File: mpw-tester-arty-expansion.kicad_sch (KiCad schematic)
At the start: 112 parts, among them J1 USB4105-GF-A, J10 61300211121, J11 61300211121, J12 61300211121, J14 61300311121, J15 61300311121, J18 61300411121, J19 61300711121, J20 61300411121, J3 Arty_A7_SPI, J4 61300211121, J5 61300311121, J6 61300211121, J7 61300211121, J8 61300211121, J9 61300211121, Q1 DTC014TEBTL, SW1 JS202011JCQN, U1 SN74LVC1G125DCKR, U2 FT232HQ, U3 SN74LVC1G125DCKR, U4 MAX811REUS+T, U5 NTS0102DP, U6 MCP4661-103E/ML, U7 Caravel_breakout_PCB, U8 W25Q32FVSS, U9 MIC2211-AAYML-TR, Y1 ABM8G-12.000MHZ-18-D2Y-T, Y2 ECS-2520MVLC-100-BN-TR

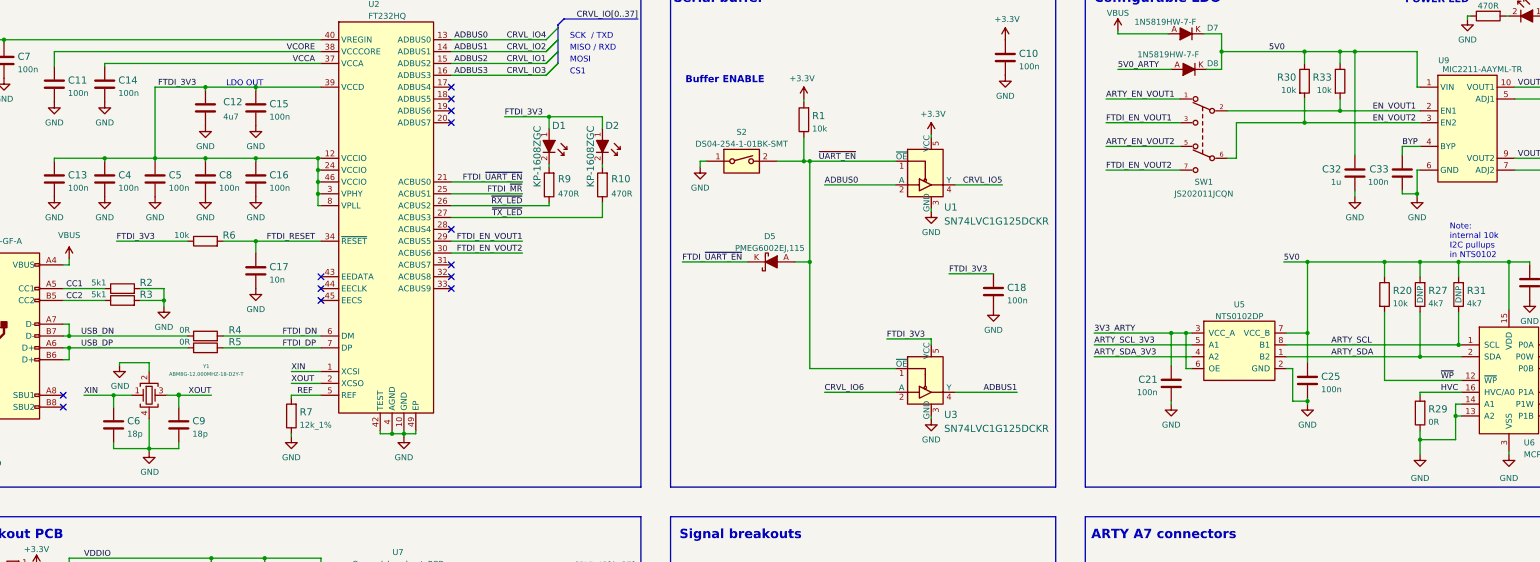
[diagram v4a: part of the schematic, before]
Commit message: Add slide switches for Arty powered from USB and UART buffer ctrl
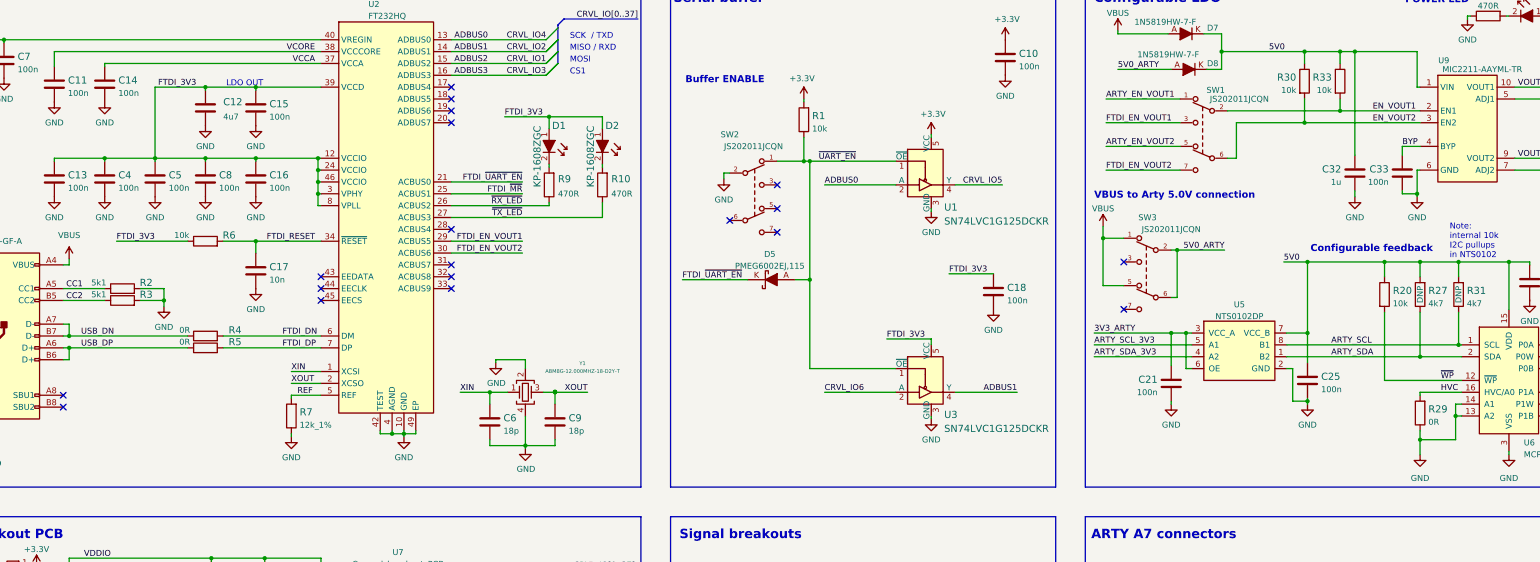
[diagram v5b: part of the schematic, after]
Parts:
- removed S2: DS04-254-1-01BK-SMT, antmicro-footprints:SW_DS04-254-1-01BK-SMT, symbol antmicroSlideSwitches:DS04-254-1-01BK-SMT
- added SW2, SW3: JS202011JCQN, antmicro-footprints:JS202011JCQN, symbol antmicroSlideSwitches:JS202011JCQN
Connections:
- net 5V0_ARTY: now also SW3.2 (1_C), SW3.6 (2_C)
- net AGND: now also SW2.2 (1_C)
- net VBUS: now also SW3.1, SW3.5
- net ~{UART_EN}: now also SW2.1
- no-connect marks 21 -> 27
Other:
- note added: "Configurable feedback"
- note added: "VBUS to Arty 5.0V connection"
- moved on the sheet: C6, C9, D5, Y1

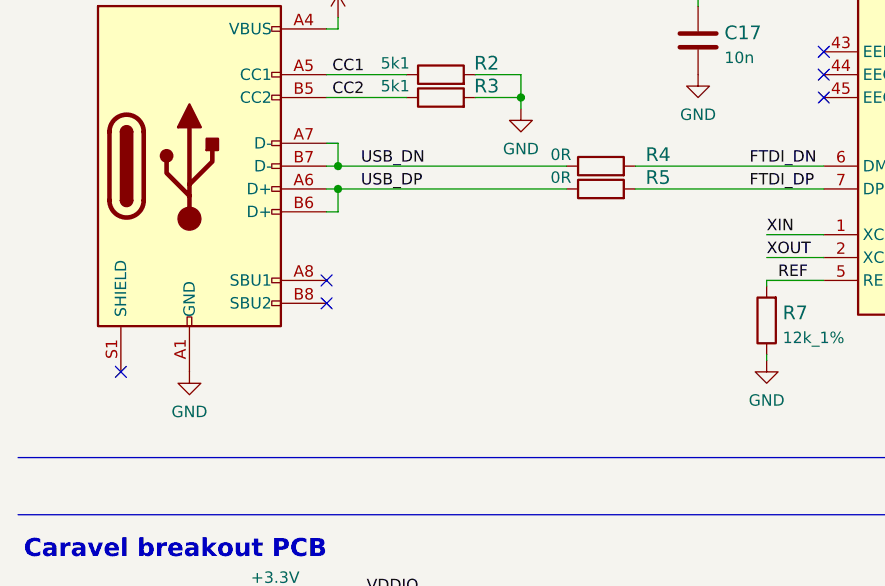
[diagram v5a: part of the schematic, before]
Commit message: Add USB TVS, finish layout, resolve DRC
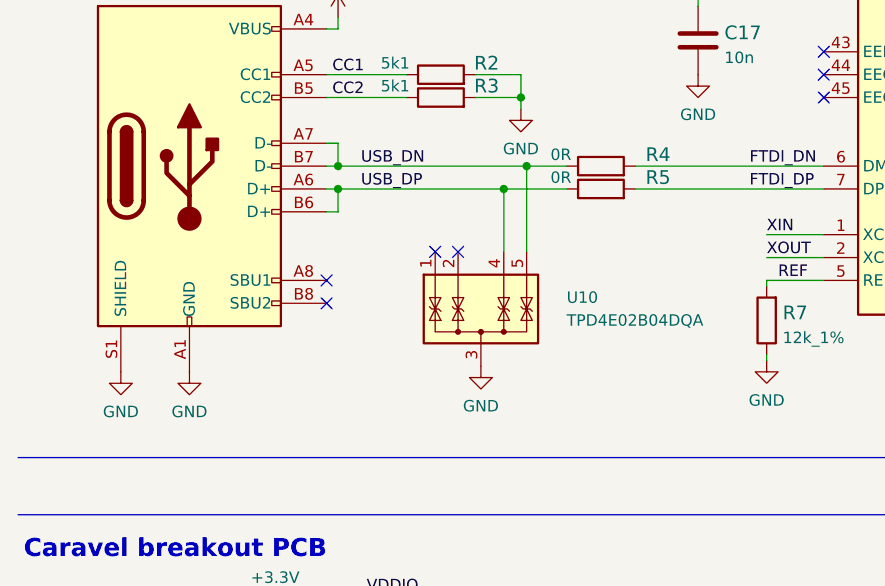
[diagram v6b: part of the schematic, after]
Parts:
- added U10: TPD4E02B04DQA, antmicro-footprints:USON-10_2.5x1.0mm_P0.5mm, symbol antmicroTVSDiodes:TPD4E02B04DQA
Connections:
- net AGND: now also J1.S1 (SHIELD), U10.3 (G), U10.8 (G)
- net USB_DN: now also U10.5 (IO4), U10.6 (NC)
- net USB_DP: now also U10.4 (IO3), U10.7 (NC)
- new net: U10.1 (IO1), U10.10 (NC)
- new net: U10.2 (IO2), U10.9 (NC)
- no-connect marks 27 -> 28
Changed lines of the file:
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@@
   (junction (at 79.375 173.355) (diameter 0) (color 0 0 0 0)
   )
+  (junction (at 69.85 88.265) (diameter 0) (color 0 0 0 0)
+  )
   (junction (at 79.375 262.255) (diameter 0) (color 0 0 0 0)
   )
@@
   (junction (at 67.945 155.575) (diameter 0) (color 0 0 0 0)
   )
+  (junction (at 67.31 90.805) (diameter 0) (color 0 0 0 0)
+  )
   (junction (at 151.765 41.275) (diameter 0) (color 0 0 0 0)
   )
@@
   (junction (at 313.69 27.305) (diameter 0) (color 0 0 0 0)
   )
-  (no_connect (at 24.765 111.125))
+  (no_connect (at 59.69 97.79))
   (no_connect (at 291.465 163.195))
   (no_connect (at 386.08 90.17))
@@
   (no_connect (at 130.81 75.565))
   (no_connect (at 130.81 34.925))
+  (no_connect (at 62.23 97.79))
   (no_connect (at 200.66 55.88))
   (no_connect (at 190.5 63.5))
@@
     (stroke (width 0) (type default) (color 0 0 0 0))
   )
+  (wire (pts (xy 67.31 90.805) (xy 74.295 90.805))
+    (stroke (width 0) (type default) (color 0 0 0 0))
+  )
   (bus (pts (xy 224.155 177.8) (xy 224.155 180.34))
     (stroke (width 0) (type default) (color 0 0 0 0))
@@
     (stroke (width 0) (type default) (color 0 0 0 0))
   )
-  (wire (pts (xy 48.895 88.265) (xy 74.295 88.265))
+  (wire (pts (xy 48.895 88.265) (xy 69.85 88.265))
     (stroke (width 0) (type default) (color 0 0 0 0))
   )
@@
     (stroke (width 0) (type default) (color 0 0 0 0))
   )
+  (wire (pts (xy 67.31 90.805) (xy 67.31 97.79))
+    (stroke (width 0) (type default) (color 0 0 0 0))
+  )
   (wire (pts (xy 59.055 259.715) (xy 60.325 259.715))
     (stroke (width 0) (type default) (color 0 0 0 0))
@@
     (stroke (width 0) (type default) (color 0 0 0 0))
   )
+  (wire (pts (xy 69.85 88.265) (xy 74.295 88.265))
+    (stroke (width 0) (type default) (color 0 0 0 0))
+  )
   (wire (pts (xy 48.895 90.805) (xy 47.625 90.805))
     (stroke (width 0) (type default) (color 0 0 0 0))
@@
     (stroke (width 0) (type default) (color 0 0 0 0))
   )
+  (wire (pts (xy 69.85 88.265) (xy 69.85 97.79))
+    (stroke (width 0) (type default) (color 0 0 0 0))
+  )
   (wire (pts (xy 227.33 147.32) (xy 245.11 147.32))
     (stroke (width 0) (type default) (color 0 0 0 0))
@@
     (stroke (width 0) (type default) (color 0 0 0 0))
   )
-  (wire (pts (xy 48.895 90.805) (xy 74.295 90.805))
+  (wire (pts (xy 48.895 90.805) (xy 67.31 90.805))
     (stroke (width 0) (type default) (color 0 0 0 0))
   )
@@
     (pin "1")
   )
+  (symbol (lib_id "power:GND") (at 24.765 111.125 0) (unit 1)
+    (in_bom yes) (on_board yes) (fields_autoplaced)
+    (property "Reference" "#PWR?" (id 0) (at 24.765 117.475 0)
+      (effects (font (size 1.27 1.27)) hide)
+    )
+    (property "Value" "GND" (id 1) (at 24.765 115.57 0))
+    (property "Footprint" "" (id 2) (at 24.765 111.125 0)
+      (effects (font (size 1.27 1.27)) hide)
+    )
+    (property "Datasheet" "" (id 3) (at 24.765 111.125 0)
+      (effects (font (size 1.27 1.27)) hide)
+    )
+    (pin "1")
+  )
   (symbol (lib_id "power:GND") (at 97.155 271.145 0) (unit 1)
     (in_bom yes) (on_board yes) (fields_autoplaced)
@@
     (pin "2")
   )
+  (symbol (lib_id "power:GND") (at 64.77 110.49 0) (unit 1)
+    (in_bom yes) (on_board yes) (fields_autoplaced)
+    (property "Reference" "#PWR0151" (id 0) (at 64.77 116.84 0)
+      (effects (font (size 1.27 1.27)) hide)
+    )
+    (property "Value" "GND" (id 1) (at 64.77 114.935 0))
+    (property "Footprint" "" (id 2) (at 64.77 110.49 0)
+      (effects (font (size 1.27 1.27)) hide)
+    )
+    (property "Datasheet" "" (id 3) (at 64.77 110.49 0)
+      (effects (font (size 1.27 1.27)) hide)
+    )
+    (pin "1")
+  )
   (symbol (lib_id "power:GND") (at 243.84 156.21 0) (mirror y) (unit 1)
     (in_bom yes) (on_board yes)
@@
     (pin "2")
   )
+  (symbol (lib_id "antmicroTVSDiodes:TPD4E02B04DQA") (at 64.77 105.41 0) (unit 1)
+    (in_bom yes) (on_board yes) (fields_autoplaced)
+    (property "Reference" "U10" (id 0) (at 74.295 102.8699 0)
+      (effects (font (size 1.27 1.27)) (justify left))
+    )
+    (property "Value" "TPD4E02B04DQA" (id 1) (at 74.295 105.4099 0)
+      (effects (font (size 1.27 1.27)) (justify left))
+    )
+    (property "Footprint" "antmicro-footprints:USON-10_2.5x1.0mm_P0.5mm" (id 2) (at 52.07 128.27 0)
+      (effects (font (size 1.27 1.27)) (justify left) hide)
+    )
+    (property "Datasheet" "http://www.ti.com/lit/ds/symlink/tpd4e02b04.pdf" (id 3) (at 64.77 125.73 0)
+      (effects (font (size 1.27 1.27)) hide)
+    )
+    (property "MPN" "TPD4E02B04DQAR" (id 4) (at 64.77 120.65 0)
+      (effects (font (size 1.27 1.27)) hide)
+    )
+    (property "Manufacturer" "Texas Instruments" (id 5) (at 64.77 123.19 0)
+      (effects (font (size 1.27 1.27)) hide)
+    )
+    (pin "3")
+    (pin "1")
+    (pin "10")
+    (pin "2")
+    (pin "4")
+    (pin "5")
+    (pin "6")
+    (pin "7")
+    (pin "8")
+    (pin "9")
+  )
   (symbol (lib_id "antmicroCapacitors0603:C_1u_0603") (at 90.805 182.88 0) (unit 1)
     (in_bom yes) (on_board yes) (fields_autoplaced)
@@
       (reference "#PWR0150") (unit 1) (value "GND") (footprint "")
     )
+    (path "/7c3d5220-0c26-4068-8fa2-00d0fffbad0b"
+      (reference "#PWR0151") (unit 1) (value "GND") (footprint "")
+    )
     (path "/3349caa0-d316-426d-823b-0e2b9b5356e8"
       (reference "#PWR0152") (unit 1) (value "GND") (footprint "")
@@
       (reference "#PWR0180") (unit 1) (value "GND") (footprint "")
     )
+    (path "/07aae223-3c13-41d7-a3d8-dbdee37fc036"
+      (reference "#PWR?") (unit 1) (value "GND") (footprint "")
+    )
     (path "/c364c452-410a-49be-b768-048ab800dd72"
       (reference "C1") (unit 1) (value "C_1u_0603") (footprint "antmicro-footprints:0603-cap")
@@
       (reference "U9") (unit 1) (value "MIC2211-AAYML-TR") (footprint "antmicro-footprints:DFN-10-1EP_3x3mm")
     )
+    (path "/df40db42-563e-400d-856d-2e4e6bd95abf"
+      (reference "U10") (unit 1) (value "TPD4E02B04DQA") (footprint "antmicro-footprints:USON-10_2.5x1.0mm_P0.5mm")
+    )
     (path "/90785e37-9e70-447f-a70d-a3ed142c95ed"

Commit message: Loclib
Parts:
- C1, C22, C23, C24, C26, C27, C28, C29, C3, C30, C31, C32, C35, C36: footprint antmicro-footprints:0603-cap -> mpw-tester-arty-expansion-footprints:0603-cap; symbol antmicroCapacitors0603:C_1u_0603 -> mpw-tester-arty-expansion:C_1u_0603
- C10, C11, C13, C14, C15, C16, C18, C19, C20, C21, C25, C33, C34, C37, C4, C5, C7, C8: footprint antmicro-footprints:0603-cap -> mpw-tester-arty-expansion-footprints:0603-cap; symbol antmicroCapacitors0603:C_100n_0603 -> mpw-tester-arty-expansion:C_100n_0603
- C12, C2: footprint antmicro-footprints:0603-cap -> mpw-tester-arty-expansion-footprints:0603-cap; symbol antmicroCapacitors0603:C_4u7_0603 -> mpw-tester-arty-expansion:C_4u7_0603
- C17: footprint antmicro-footprints:0603-cap -> mpw-tester-arty-expansion-footprints:0603-cap; symbol antmicroCapacitors0603:C_10n_0603 -> mpw-tester-arty-expansion:C_10n_0603
- C6, C9: footprint antmicro-footprints:0603-cap -> mpw-tester-arty-expansion-footprints:0603-cap; symbol antmicroCapacitors0603:C_18p_0603 -> mpw-tester-arty-expansion:C_18p_0603
- D1, D2, D3, D4: footprint antmicro-footprints:LED_0603 -> mpw-tester-arty-expansion-footprints:LED_0603; symbol antmicroLEDIndicationDiscrete:KP-1608ZGC -> mpw-tester-arty-expansion:KP-1608ZGC
- D5, D6, D9: footprint antmicro-footprints:SOD-323F -> mpw-tester-arty-expansion-footprints:SOD-323F; symbol antmicroDiodesRectifiersSingle:PMEG6002EJ,115 -> mpw-tester-arty-expansion:PMEG6002EJ,115
- D7, D8: footprint antmicro-footprints:SOD-123 -> mpw-tester-arty-expansion-footprints:SOD-123; symbol antmicroDiodesRectifiersSingle:1N5819HW-7-F -> mpw-tester-arty-expansion:1N5819HW-7-F
- J1: footprint antmicro-footprints:GCT_USB4105-GF-A -> mpw-tester-arty-expansion-footprints:GCT_USB4105-GF-A; symbol antmicroUSBDVIHDMIConnectors:USB4105-GF-A -> mpw-tester-arty-expansion:USB4105-GF-A
- J10, J11, J12, J4, J6, J7, J8, J9: footprint antmicro-footprints:PinHeader_1x2_P2.54_Drill0.9mm -> mpw-tester-arty-expansion-footprints:PinHeader_1x2_P2.54_Drill0.9mm; symbol antmicroRectangularConnectorsHeadersMalePins:61300211121 -> mpw-tester-arty-expansion:61300211121
- J14, J15, J5: footprint antmicro-footprints:PinHeader_1x3_P2.54_Drill1.1mm -> mpw-tester-arty-expansion-footprints:PinHeader_1x3_P2.54_Drill1.1mm; symbol antmicroRectangularConnectorsHeadersMalePins:61300311121 -> mpw-tester-arty-expansion:61300311121
- J18, J20: footprint antmicro-footprints:PinHeader_1x4_P2.54mm_Drill1.02mm -> mpw-tester-arty-expansion-footprints:PinHeader_1x4_P2.54mm_Drill1.02mm; symbol antmicroRectangularConnectorsHeadersMalePins:61300411121 -> mpw-tester-arty-expansion:61300411121
- J19: footprint antmicro-footprints:61300711121 -> mpw-tester-arty-expansion-footprints:61300711121; symbol antmicroRectangularConnectorsHeadersMalePins:61300711121 -> mpw-tester-arty-expansion:61300711121
- J3: footprint antmicro-footprints:ARTY_A7_SHIELD -> mpw-tester-arty-expansion-footprints:ARTY_A7_SHIELD; symbol antmicroRectangularConnectorsHeadersMalePins:Arty_A7_SPI -> mpw-tester-arty-expansion:Arty_A7_SPI
- Q1: footprint antmicro-footprints:SOT-416 -> mpw-tester-arty-expansion-footprints:SOT-416; symbol antmicroTransistorsBipolarSingle:DTC014TEBTL -> mpw-tester-arty-expansion:DTC014TEBTL
- R1, R16, R17, R18, R19, R20, R21, R26, R28, R30, R32, R33, R34, R6: footprint antmicro-footprints:0603-res -> mpw-tester-arty-expansion-footprints:0603-res; symbol antmicroResistors0603:R_10k_0603 -> mpw-tester-arty-expansion:R_10k_0603
- R10, R12, R13, R9: footprint antmicro-footprints:0603-res -> mpw-tester-arty-expansion-footprints:0603-res; symbol antmicroResistors0603:R_470R_0603 -> mpw-tester-arty-expansion:R_470R_0603
- R11, R14, R15, R29, R8: footprint antmicro-footprints:0603-res -> mpw-tester-arty-expansion-footprints:0603-res; symbol antmicroResistors0603:R_0R_0603 -> mpw-tester-arty-expansion:R_0R_0603
- R2, R3: footprint antmicro-footprints:0603-res -> mpw-tester-arty-expansion-footprints:0603-res; symbol antmicroResistors0603:R_5k1_0603 -> mpw-tester-arty-expansion:R_5k1_0603
- R22: footprint antmicro-footprints:0603-res -> mpw-tester-arty-expansion-footprints:0603-res; symbol antmicroResistors0603:R_68k_0603 -> mpw-tester-arty-expansion:R_68k_0603
- R23: footprint antmicro-footprints:0603-res -> mpw-tester-arty-expansion-footprints:0603-res; symbol antmicroResistors0603:R_41k2_0603 -> mpw-tester-arty-expansion:R_41k2_0603
- R24: footprint antmicro-footprints:0603-res -> mpw-tester-arty-expansion-footprints:0603-res; symbol antmicroResistors0603:R_15k_0603 -> mpw-tester-arty-expansion:R_15k_0603
- R25: footprint antmicro-footprints:0603-res -> mpw-tester-arty-expansion-footprints:0603-res; symbol antmicroResistors0603:R_34k_0603 -> mpw-tester-arty-expansion:R_34k_0603
- R27, R31: footprint antmicro-footprints:0603-res -> mpw-tester-arty-expansion-footprints:0603-res; symbol antmicroResistors0603:R_4k7_0603 -> mpw-tester-arty-expansion:R_4k7_0603
- R4, R5: footprint antmicro-footprints:0402-res -> mpw-tester-arty-expansion-footprints:0402-res; symbol antmicroResistors0402:R_0R_0402 -> mpw-tester-arty-expansion:R_0R_0402
- R7: footprint antmicro-footprints:0603-res -> mpw-tester-arty-expansion-footprints:0603-res; symbol antmicroResistors0603:R_12k_1%_0603 -> mpw-tester-arty-expansion:R_12k_1%_0603
- S1: footprint antmicro-footprints:SW_SPST_4.2x2.8 -> mpw-tester-arty-expansion-footprints:SW_SPST_4.2x2.8; symbol antmicroPushbuttonSwitches:KMR2 -> mpw-tester-arty-expansion:KMR2
- SW1, SW2, SW3: footprint antmicro-footprints:JS202011JCQN -> mpw-tester-arty-expansion-footprints:JS202011JCQN; symbol antmicroSlideSwitches:JS202011JCQN -> mpw-tester-arty-expansion:JS202011JCQN
- TP1: footprint antmicro-footprints:PROBE_PAD_1206 -> mpw-tester-arty-expansion-footprints:PROBE_PAD_1206; symbol antmicroTestPoints:RCW-0C -> mpw-tester-arty-expansion:RCW-0C
- U1, U3: footprint antmicro-footprints:SOT-353 -> mpw-tester-arty-expansion-footprints:SOT-353; symbol antmicroLogicBuffersDriversReceiversTransceivers:SN74LVC1G125DCKR -> mpw-tester-arty-expansion:SN74LVC1G125DCKR
- U10: footprint antmicro-footprints:USON-10_2.5x1.0mm_P0.5mm -> mpw-tester-arty-expansion-footprints:USON-10_2.5x1.0mm_P0.5mm; symbol antmicroTVSDiodes:TPD4E02B04DQA -> mpw-tester-arty-expansion:TPD4E02B04DQA
- U2: footprint antmicro-footprints:QFN-48-1EP_8x8mm_P0.5mm_EP6.2x6.2mm_FT232HQ_marking -> mpw-tester-arty-expansion-footprints:QFN-48-1EP_8x8mm_P0.5mm_EP6.2x6.2mm_FT232HQ_marking; symbol antmicroInterfaceControllers:FT232HQ -> mpw-tester-arty-expansion:FT232HQ
- U4: footprint antmicro-footprints:SOT-143-4 -> mpw-tester-arty-expansion-footprints:SOT-143-4; symbol antmicroPMICPowerSequencers:MAX811REUS+T -> mpw-tester-arty-expansion:MAX811REUS+T
- U5: footprint antmicro-footprints:TSSOP-8_W3mm -> mpw-tester-arty-expansion-footprints:TSSOP-8_W3mm; symbol antmicroLogicTranslatorsLevelShifters:NTS0102DP -> mpw-tester-arty-expansion:NTS0102DP
- U6: footprint antmicro-footprints:QFN-16_EP_4x4_Pitch0.65mm -> mpw-tester-arty-expansion-footprints:QFN-16_EP_4x4_Pitch0.65mm; symbol antmicroInterfaceIOExpanders:MCP4661-103E/ML -> mpw-tester-arty-expansion:MCP4661-103E/ML
- U7: footprint antmicro-footprints:caravel_breakout -> mpw-tester-arty-expansion-footprints:caravel_breakout; symbol antmicroModules:Caravel_breakout_PCB -> mpw-tester-arty-expansion:Caravel_breakout_PCB
- U8: footprint antmicro-footprints:SOIC127P790X216-8N -> mpw-tester-arty-expansion-footprints:SOIC127P790X216-8N; symbol antmicroMemory:W25Q32FVSS -> mpw-tester-arty-expansion:W25Q32FVSS
- U9: footprint antmicro-footprints:DFN-10-1EP_3x3mm -> mpw-tester-arty-expansion-footprints:DFN-10-1EP_3x3mm; symbol antmicroPMICVoltageRegulatorsLinear:MIC2211-AAYML-TR -> mpw-tester-arty-expansion:MIC2211-AAYML-TR
- Y1: footprint antmicro-footprints:KX-7 -> mpw-tester-arty-expansion-footprints:KX-7; symbol antmicroCrystals:ABM8G-12.000MHZ-18-D2Y-T -> mpw-tester-arty-expansion:ABM8G-12.000MHZ-18-D2Y-T
- Y2: footprint antmicro-footprints:Oscillator_SMD_ECS_2520MV-xxx-xx-4Pin_2.5x2.0mm -> mpw-tester-arty-expansion-footprints:Oscillator_SMD_ECS_2520MV-xxx-xx-4Pin_2.5x2.0mm; symbol antmicroCrystals:ECS-2520MVLC-100-BN-TR -> mpw-tester-arty-expansion:ECS-2520MVLC-100-BN-TR
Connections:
- net ADBUS0: no longer J3.35 (IO37)
- net ADBUS1: no longer J3.34 (IO38)
- net ADBUS2: no longer J3.51 (IO13)
- net ADBUS3: no longer J3.52 (IO12)
- net ARTY_SCL_3V3: no longer J3.47 (SCL)
- net ARTY_SDA_3V3: no longer J3.48 (SDA)
- net ARTY_XCLK: no longer J3.32 (IO40)
- net ARTY_~{MR}: no longer J3.31 (IO41)
- net CRVL_IO0: no longer J3.33 (IO39)
- net CRVL_IO10: no longer J3.38 (IO34)
- net CRVL_IO11: no longer J3.56 (IO08)
- net CRVL_IO12: no longer J3.39 (IO33)
- net CRVL_IO13: no longer J3.57 (IO07)
- net CRVL_IO14: no longer J3.40 (IO32)
- net CRVL_IO15: no longer J3.58 (IO06)
- net CRVL_IO16: no longer J3.41 (IO31)
- net CRVL_IO17: no longer J3.59 (IO05)
- net CRVL_IO18: no longer J3.42 (IO30)
- net CRVL_IO19: no longer J3.60 (IO04)
- net CRVL_IO20: no longer J3.43 (IO29)
- net CRVL_IO21: no longer J3.61 (IO03)
- net CRVL_IO22: no longer J3.44 (IO28)
- net CRVL_IO23: no longer J3.62 (IO02)
- net CRVL_IO24: no longer J3.45 (IO27)
- net CRVL_IO25: no longer J3.63 (IO01)
- net CRVL_IO26: no longer J3.46 (IO26)
- net CRVL_IO27: no longer J3.64 (IO00)
- net CRVL_IO5: no longer J3.53 (IO11)
- net CRVL_IO6: no longer J3.36 (IO36)
- net CRVL_IO7: no longer J3.54 (IO10)
- net CRVL_IO8: no longer J3.37 (IO35)
- net CRVL_IO9: no longer J3.55 (IO09)

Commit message: Fix Arty symbol, add EP pin to MIC221 and MCP4661 symbols
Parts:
- removed J3: Arty_A7_SPI, mpw-tester-arty-expansion-footprints:ARTY_A7_SHIELD, symbol mpw-tester-arty-expansion:Arty_A7_SPI
- added J3: arty_chipKIT_connector, mpw-tester-arty-expansion-footprints:ARTY_A7_SHIELD, symbol mpw-tester-arty-expansion:arty_chipKIT_connector
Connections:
- net 3V3_ARTY: now also J3.4 (3V3)
- net 5V0_ARTY: now also J3.5 (5V)
- net ADBUS0: now also J3.35 (IO37)
- net ADBUS1: now also J3.34 (IO38)
- net ADBUS2: now also J3.51 (IO13)
- net ADBUS3: now also J3.52 (IO12)
- net AGND: now also U6.17 (EP), U9.11 (EP), J3.17 (XGND), J3.26 (GND), J3.6 (GND), J3.7 (GND)
- net ARTY_EN_VOUT1: now also J3.9 (A0)
- net ARTY_EN_VOUT2: now also J3.19 (A6)
- net ARTY_MEM_CS: now also J3.25 (SS)
- net ARTY_MEM_MISO: now also R14.1, J3.28 (MISO); no longer R15.1
- net ARTY_MEM_MOSI: now also R15.1, J3.29 (MOSI); no longer R14.1
- net ARTY_MEM_SCK: now also J3.27 (SCK)
- net ARTY_SCL_3V3: now also J3.47 (SCL)
- net ARTY_SDA_3V3: now also J3.48 (SDA)
- net ARTY_XCLK: now also J3.32 (IO40)
- net ARTY_~{MR}: now also J3.31 (IO41)
- net CRVL_IO0: now also J3.33 (IO39)
- net CRVL_IO10: now also J3.38 (IO34)
- net CRVL_IO11: now also J3.56 (IO08)
- net CRVL_IO12: now also J3.39 (IO33)
- net CRVL_IO13: now also J3.57 (IO07)
- net CRVL_IO14: now also J3.40 (IO32)
- net CRVL_IO15: now also J3.58 (IO06)
- net CRVL_IO16: now also J3.41 (IO31)
- net CRVL_IO17: now also J3.59 (IO05)
- net CRVL_IO18: now also J3.42 (IO30)
- net CRVL_IO19: now also J3.60 (IO04)
- net CRVL_IO20: now also J3.43 (IO29)
- net CRVL_IO21: now also J3.61 (IO03)
- net CRVL_IO22: now also J3.44 (IO28)
- net CRVL_IO23: now also J3.62 (IO02)
- net CRVL_IO24: now also J3.45 (IO27)
- net CRVL_IO25: now also J3.63 (IO01)
- net CRVL_IO26: now also J3.46 (IO26)
- net CRVL_IO27: now also J3.64 (IO00)
- net CRVL_IO28: now also J3.24 (A11)
- net CRVL_IO29: now also J3.14 (A5)
- net CRVL_IO30: now also J3.23 (A10)
- net CRVL_IO31: now also J3.13 (A4)
- net CRVL_IO32: now also J3.22 (A9)
- net CRVL_IO33: now also J3.12 (A3)
- net CRVL_IO34: now also J3.21 (A8)
- net CRVL_IO35: now also J3.11 (A2)
- net CRVL_IO36: now also J3.20 (A7)
- net CRVL_IO37: now also J3.10 (A1)
- net CRVL_IO5: now also J3.53 (IO11)
- net CRVL_IO6: now also J3.36 (IO36)
- net CRVL_IO7: now also J3.54 (IO10)
- net CRVL_IO8: now also J3.37 (IO35)
- net CRVL_IO9: now also J3.55 (IO09)
- net MEM.SI: now also R15.2; no longer R14.2
- net MEM.SO: now also R14.2; no longer R15.2
- no-connect marks 28 -> 29
